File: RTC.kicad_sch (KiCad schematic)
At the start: 14 parts, among them J8 Molex 470531000, U5 PCF85063AT/AAZ, U6 EMC2301-1-ACZL-TR, U7 74LVC1G07SE-7

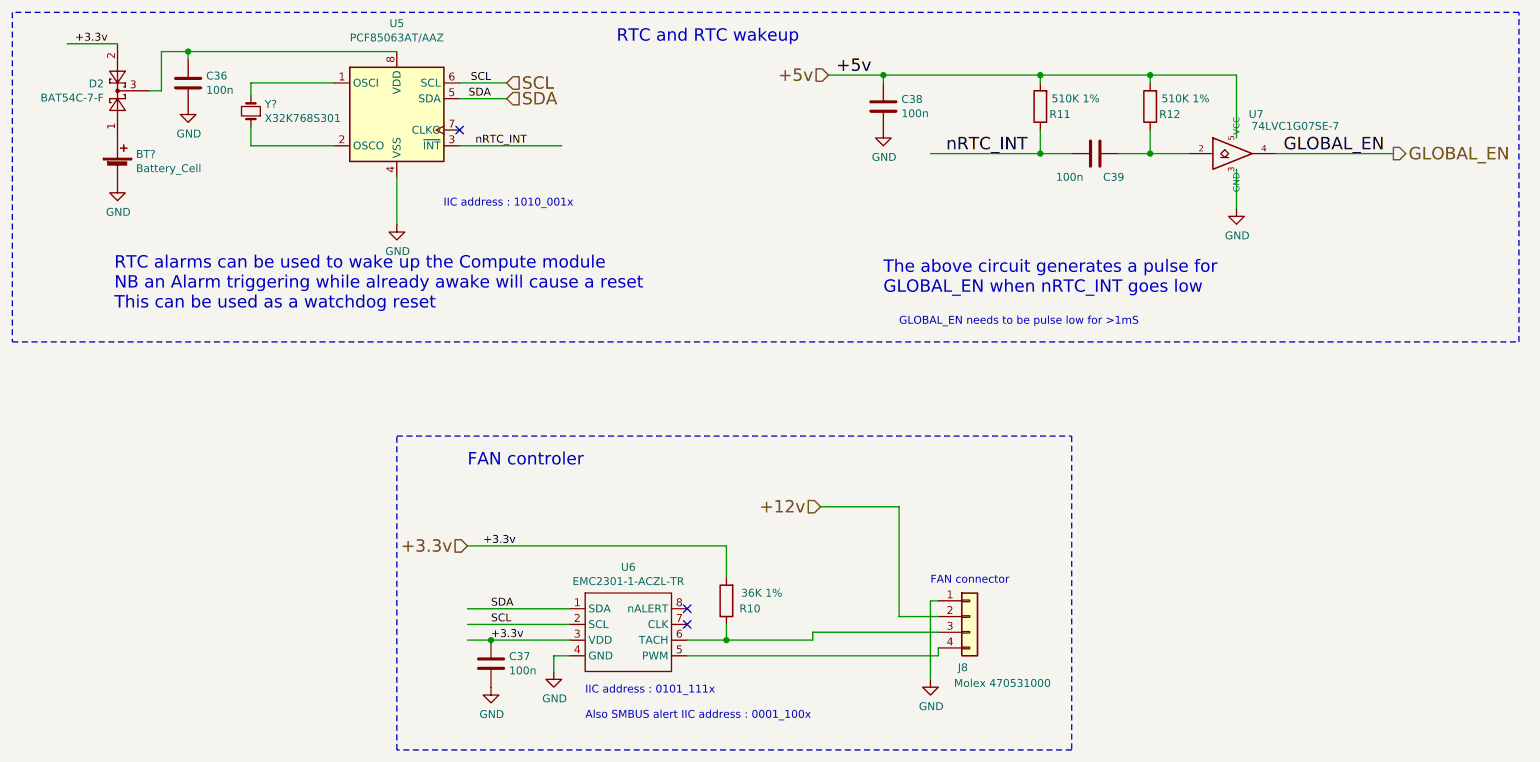
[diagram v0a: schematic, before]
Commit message: Cleaned up schematics and added gnds and no-connects
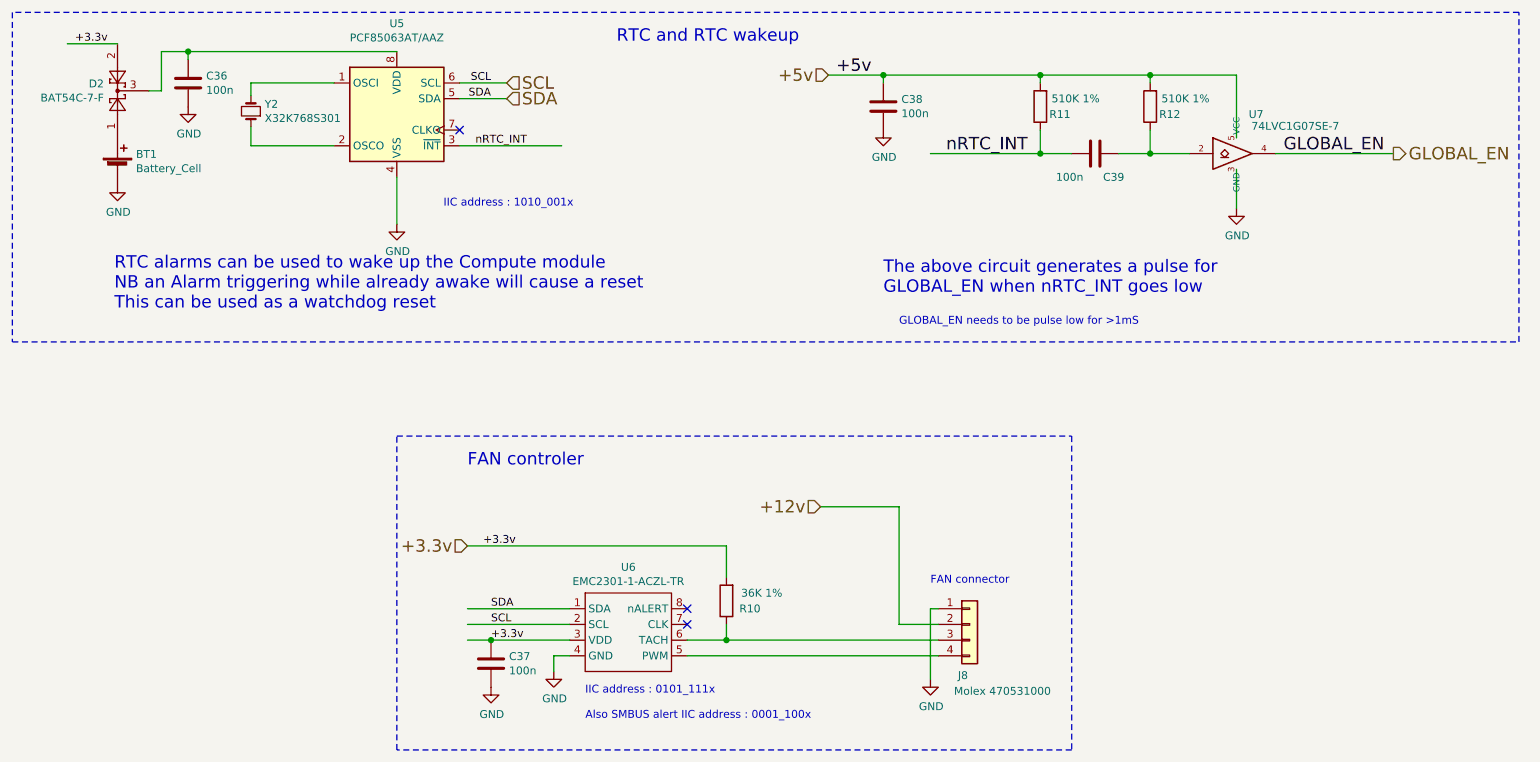
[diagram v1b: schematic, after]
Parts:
- gave numbers to parts that had none: 2
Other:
- moved on the sheet: J8
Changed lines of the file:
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@@
-	(wire
-		(pts
-			(xy 156.21 137.16) (xy 156.21 138.43)
-		)
-		(stroke
-			(width 0)
-			(type solid)
-		)
-	)
 	(wire
 		(pts
@@
 	(wire
 		(pts
-			(xy 175.26 132.08) (xy 175.26 144.78)
+			(xy 175.26 133.35) (xy 175.26 144.78)
 		)
 		(stroke
@@
 	(wire
 		(pts
-			(xy 176.53 132.08) (xy 175.26 132.08)
+			(xy 176.53 133.35) (xy 175.26 133.35)
 		)
 		(stroke
@@
 	(wire
 		(pts
-			(xy 142.24 138.43) (xy 156.21 138.43)
+			(xy 142.24 138.43) (xy 176.53 138.43)
 		)
 		(stroke
@@
 	(wire
 		(pts
-			(xy 176.53 134.62) (xy 170.18 134.62)
+			(xy 176.53 135.89) (xy 170.18 135.89)
 		)
 		(stroke
@@
 	(wire
 		(pts
-			(xy 170.18 116.84) (xy 170.18 134.62)
+			(xy 170.18 116.84) (xy 170.18 135.89)
 		)
 		(stroke
@@
 		)
 	)
-	(wire
-		(pts
-			(xy 176.53 137.16) (xy 156.21 137.16)
-		)
-		(stroke
-			(width 0)
-			(type solid)
-		)
-	)
 	(polyline
 		(pts
@@
 		(pts
 			(xy 193.04 46.99) (xy 210.82 46.99)
-		)
-		(stroke
-			(width 0)
-			(type solid)
-		)
-	)
-	(wire
-		(pts
-			(xy 176.53 140.97) (xy 176.53 139.7)
 		)
 		(stroke
@@
 		(on_board yes)
 		(dnp no)
-		(property "Reference" "BT?"
+		(property "Reference" "BT1"
 			(at 46.6852 59.7916 0)
 			(effects
@@
 			(project "ANE21_PCB"
 				(path "/27bae9d5-8d47-4d02-9c9d-2650041a529b/2c41d5bd-5192-4bc8-a076-4ff2f00d6f05"
-					(reference "BT?")
+					(reference "BT1")
 					(unit 1)
 				)
@@
 		(on_board yes)
 		(dnp no)
-		(property "Reference" "Y?"
+		(property "Reference" "Y2"
 			(at 67.5132 51.689 90)
 			(effects
@@
 			(project "ANE21_PCB"
 				(path "/27bae9d5-8d47-4d02-9c9d-2650041a529b/2c41d5bd-5192-4bc8-a076-4ff2f00d6f05"
-					(reference "Y?")
+					(reference "Y2")
 					(unit 1)
 				)
@@
 	(symbol
 		(lib_id "Connector_Generic:Conn_01x04")
-		(at 181.61 134.62 0)
+		(at 181.61 135.89 0)
 		(unit 1)
 		(exclude_from_sim no)
@@
 		(dnp no)
 		(property "Reference" "J8"
-			(at 179.705 142.875 0)
+			(at 179.705 144.145 0)
 			(effects
 				(font
@@
 		)
 		(property "Value" "Molex 470531000"
-			(at 179.07 145.415 0)
+			(at 179.07 146.685 0)
 			(effects
 				(font
@@
 		)
 		(property "Footprint" "Connector:FanPinHeader_1x04_P2.54mm_Vertical"
-			(at 181.61 134.62 0)
+			(at 181.61 135.89 0)
 			(effects
 				(font
@@
 		)
 		(property "Datasheet" "https://www.molex.com/pdm_docs/sd/470531000_sd.pdf"
-			(at 181.61 134.62 0)
+			(at 181.61 135.89 0)
 			(effects
 				(font
@@
 		)
 		(property "Description" ""
-			(at 181.61 134.62 0)
+			(at 181.61 135.89 0)
 			(effects
 				(font
@@
 		)
 		(property "Field4" "Farnell"
-			(at 181.61 134.62 0)
+			(at 181.61 135.89 0)
 			(effects
 				(font
@@
 		)
 		(property "Field5" "	2313705"
-			(at 181.61 134.62 0)
+			(at 181.61 135.89 0)
 			(effects
 				(font
@@
 		)
 		(property "Field6" "470531000"
-			(at 181.61 134.62 0)
+			(at 181.61 135.89 0)
 			(effects
 				(font
@@
 		)
 		(property "Field7" "Molex"
-			(at 181.61 134.62 0)
+			(at 181.61 135.89 0)
 			(effects
 				(font
@@
 		)
 		(property "Part Description" "	Connector Header Through Hole 4 position 0.100\" (2.54mm)"
-			(at 181.61 134.62 0)
-			(effects
-				(font
+			(at 181.61 135.89 0)
+			(effects
+				(font

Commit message: Added 3d-models, esd protection, cleaned up and made small start with pcb
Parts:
- U7: footprint Package_TO_SOT_SMD:SOT-353_SC-70-5 -> 74LVC1G07SE-7:SOT65P210X110-5N
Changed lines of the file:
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@@
 			)
 		)
-		(property "Footprint" "Package_TO_SOT_SMD:SOT-353_SC-70-5"
+		(property "Footprint" "74LVC1G07SE-7:SOT65P210X110-5N"
 			(at 224.79 59.69 0)
 			(effects
